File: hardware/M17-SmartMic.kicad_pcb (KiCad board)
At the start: 4 copper layers, 100 x 80 mm, 193 parts, among them IC301 LM4991xx, J301 CAT_TX, J302 CAT_TX, J401 Radio, J402 USB_C, J403 Radio_Opt, J404 Kenwood-3.5, J405 Kenwood-2.5, J406 OLED, J407 KH-RJ45-58-8P8C, J408 STLink, J409 UART, J410 Speaker, J411 +12V, Q201 MMBT3904, Q202 IRLML2244, Q301 IRLML2060, Q302 BSS138, Q303 BSS138, SW201 Button Power, SW202 Reset, SW203 Button Enter, SW204 Button Left, SW205 Button Up, SW206 Button Down, SW207 Button Escape, SW208 Button Right, U201 STM32F405RGTx, U202 TPS7A2033, U203 TP6841S6, U301 MCP6002, U302 MAX9814, U401 USBLC6-2, U501 MCP4551-103, U502 MCP455x, U503 MCP6002, U504 MCP6002, Y201 8 MHz

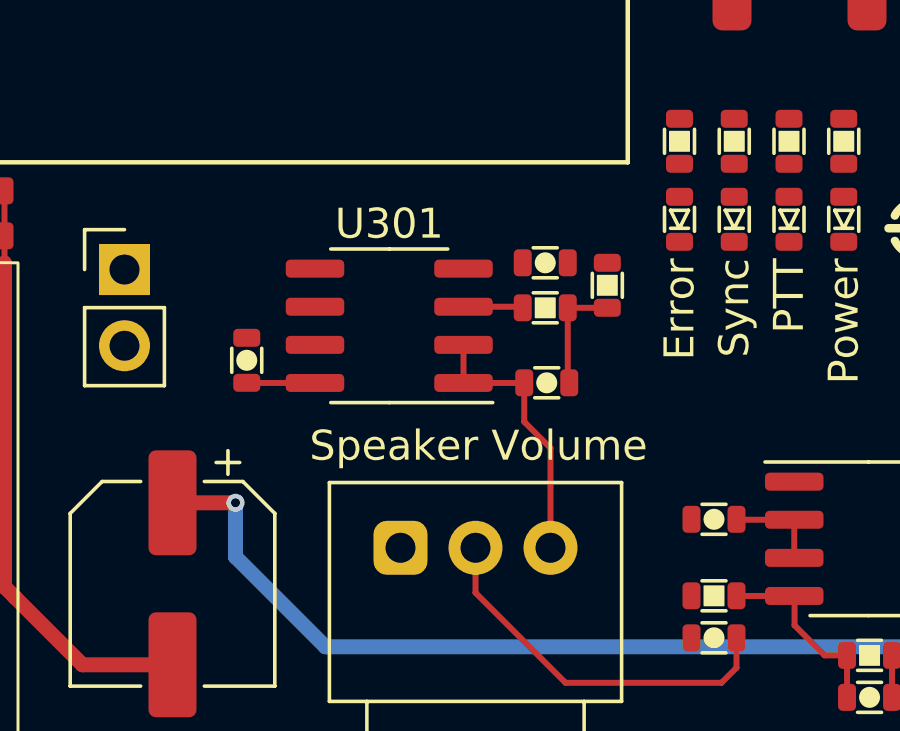
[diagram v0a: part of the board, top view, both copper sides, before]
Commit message: Updated audio output stage
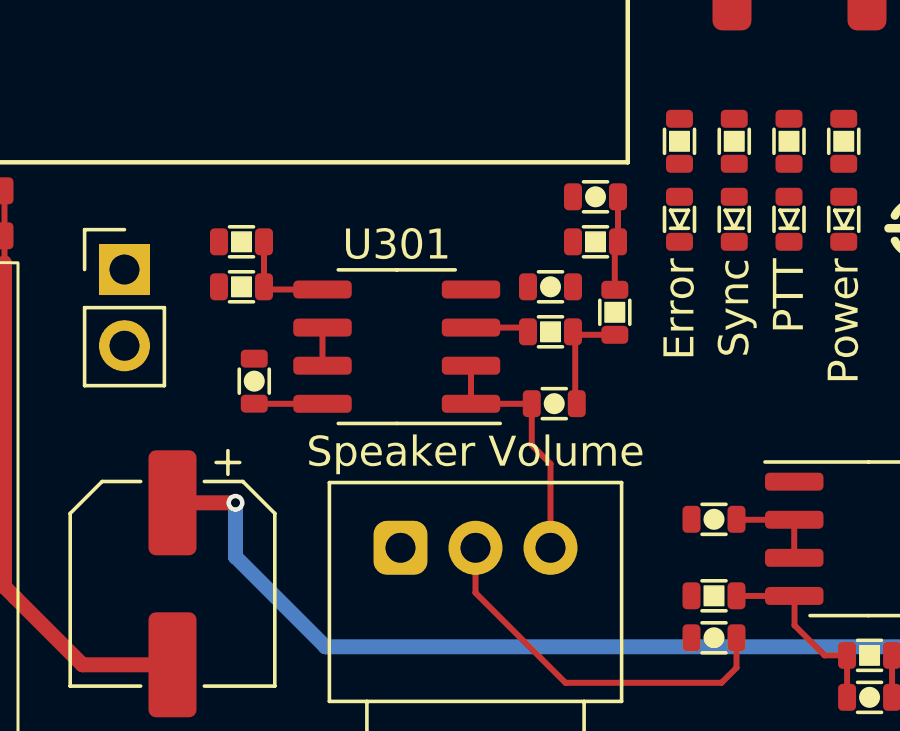
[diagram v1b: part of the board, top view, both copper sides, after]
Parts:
- added C315: 4u7, pkl_dipol:C_0603, F.Cu at (136.5, 120.8)
- added R316: 9k1, pkl_dipol:R_0603, F.Cu at (136.5, 122.3)
- added R317: 10k, pkl_dipol:R_0603, F.Cu at (124.7, 122.3)
- added R318: 10k, pkl_dipol:R_0603, F.Cu at (124.7, 123.8)
- C303: value 4.7n -> 220n
- C304: value 10n -> 1u5
- R303: value 7.5k -> 130k
- R304: value 4.7k -> 36k
- R307: value 1k8 -> 3k3
- moved R303 0.93 mm to (137.1, 124.7)
- moved C303 0.82 mm to (135.0, 123.8)
- moved R304 0.82 mm to (135.0, 125.3)
- moved U301 0.74 mm to (129.9, 125.8)
- moved C302 0.74 mm to (125.1, 126.9)
- moved C304 0.74 mm to (135.1, 127.7)
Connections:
- R303 pad 1: AUDIO_SPK -> Net-(C315-Pad1)
- U301 pad 5: unconnected-(U301B-+-Pad5) -> Net-(U301B-+)
- U301 pad 6: unconnected-(U301B---Pad6) -> Net-(U301B--)
- U301 pad 7: unconnected-(U301-Pad7) -> Net-(U301B--)
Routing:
- net Net-(U301B-+): track 0.00 -> 3.49 mm
- net Net-(C315-Pad1): track 0.00 -> 3.14 mm
- net Net-(U301B--): track 0.00 -> 1.27 mm
- net Net-(U301A--): track 9.16 -> 8.36 mm

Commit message: PCB Layout
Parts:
- added C226: 100n, pkl_dipol:C_0603, F.Cu at (75.0, 102.1)
- added C227: 10n, pkl_dipol:C_0603, F.Cu at (75.0, 103.5)
- added FB204: FB0805, pkl_dipol:L_0805, F.Cu at (68.8, 102.9)
- added FB401: FB0805, pkl_dipol:L_0805, F.Cu at (111.9, 75.3)
- added JP201: Jumper_2_Bridged, Connector_PinHeader_2.54mm:PinHeader_1x02_P2.54mm_Vertical, F.Cu at (101.9, 84.4)
- added L202: 5u, pkl_dipol:L_0805, F.Cu at (205.8, 63.9)
- J302: value CAT_TX -> CAT_RX
- moved TP303 143.0 mm to (37.4, 107.2)
- moved TP304 142.8 mm to (28.0, 102.8)
- moved TP501 134.3 mm to (33.1, 104.5)
- moved TP502 128.5 mm to (29.9, 106.0)
- moved R202 120.0 mm to (207.0, 87.0)
- moved C223 80.3 mm to (210.0, 63.7)
- moved TP301 67.2 mm to (122.8, 149.6)
- moved FB201 62.4 mm to (124.7, 75.6), turned to 0 degrees
- moved TP302 40.1 mm to (123.0, 153.4)
- moved J410 28.0 mm to (92.8, 125.2), turned to 90 degrees
- moved C301 27.6 mm to (81.0, 97.0)
- moved Q301 27.6 mm to (78.4, 97.0)
- moved R301 27.6 mm to (83.1, 96.2)
- moved R302 27.6 mm to (83.1, 97.8)
- moved TP504 22.0 mm to (35.2, 97.3)
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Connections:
- C213 pad 1: VDD -> /MCU & Power/VDD_MCU
- C214 pad 1: VDD -> /MCU & Power/VDD_MCU
- C216 pad 1: VDD -> /MCU & Power/VDD_MCU
- C217 pad 1: VDD -> /MCU & Power/VDD_MCU
- C219 pad 1: VDD -> /MCU & Power/VDD_MCU
- C221 pad 1: VDD -> /MCU & Power/VDD_MCU
- C222 pad 1: VDD -> /MCU & Power/VDD_MCU
- C223 pad 1: VAA -> Net-(JP201-A)
- D203 pad 1: +5V -> Net-(D203-K)
- D401 pad 1: +5V -> Net-(D401-K)
- FB201 pad 1: +12V -> Net-(Q202-S)
- FB201 pad 2: Net-(Q202-D) -> VIN
- Q202 pad 2: VIN -> Net-(Q202-S)
- Q202 pad 3: Net-(Q202-D) -> +12V
- R205 pad 1: VIN -> Net-(Q202-S)
- SW201 pad 1: VIN -> Net-(Q202-S)
- U201 pad 1: VBAT -> unconnected-(U201-VBAT-Pad1)
- U201 pad 19: VDD -> /MCU & Power/VDD_MCU
- U201 pad 32: VDD -> /MCU & Power/VDD_MCU
- U201 pad 48: VDD -> /MCU & Power/VDD_MCU
- U201 pad 64: VDD -> /MCU & Power/VDD_MCU
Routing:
- net BTN_DOWN: track 0.00 -> 94.9 mm, vias 0 -> 2
- net BTN_LEFT: track 0.00 -> 91.2 mm, vias 0 -> 2
- net BTN_RIGHT: track 0.00 -> 87.8 mm, vias 0 -> 2
- net ~{BOOT0}: track 0.00 -> 83.3 mm, vias 0 -> 2
- net BTN_UP: track 0.00 -> 76.9 mm, vias 0 -> 2
- net BTN_ENT: track 0.00 -> 72.0 mm, vias 0 -> 2
- net SPK_MUTE: track 0.00 -> 70.6 mm, vias 0 -> 2
- net ~{PTT_IN}: track 2.90 -> 69.0 mm, vias 0 -> 3
- net AUDIO_SPK: track 0.00 -> 64.9 mm, vias 0 -> 2
- net LED-ERROR: track 0.00 -> 63.0 mm, vias 0 -> 2
- net VDD: track 3.87 -> 65.8 mm
- net LED-SYNC: track 0.00 -> 60.9 mm, vias 0 -> 2
- net LED-PTT: track 0.00 -> 58.8 mm, vias 0 -> 2
- net USB_DN: track 0.00 -> 57.5 mm
- net USB_DP: track 0.00 -> 56.8 mm
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- added copper zone on F.Cu, net GND

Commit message: PCB Layout [WIP]
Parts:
- moved C223 137.9 mm to (75.7, 94.8), turned to 180 degrees
- moved R201 137.6 mm to (78.9, 82.2), turned to 0 degrees
- moved C211 135.3 mm to (80.3, 94.5), turned to -90 degrees
- moved C209 134.8 mm to (79.7, 91.7), turned to 90 degrees
- moved L202 133.3 mm to (75.7, 92.7), turned to 180 degrees
- moved C206 129.3 mm to (83.4, 94.7), turned to 180 degrees
- moved R204 127.9 mm to (82.1, 83.5), turned to 90 degrees
- moved U202 127.8 mm to (83.6, 91.8), turned to 180 degrees
- moved R202 127.8 mm to (79.4, 80.1), turned to -90 degrees
- moved D202 127.0 mm to (82.3, 80.3), turned to 0 degrees
- moved Q201 126.9 mm to (82.8, 86.7), turned to -90 degrees
- moved R203 125.1 mm to (83.5, 83.5), turned to -90 degrees
- moved C208 122.4 mm to (86.4, 92.0), turned to 90 degrees
- moved R206 121.8 mm to (85.4, 86.9), turned to -90 degrees
- moved R205 119.8 mm to (86.2, 84.7), turned to 180 degrees
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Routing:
- net BASEBAND_RX: track 0.00 -> 105.8 mm, vias 0 -> 2
- net I2C_SDA: track 0.00 -> 93.4 mm, vias 0 -> 3
- net I2C_SCL: track 0.00 -> 93.1 mm, vias 0 -> 3
- net BASEBAND_TX: track 0.00 -> 92.4 mm, vias 0 -> 2
- net Net-(Q202-S): track 7.96 -> 64.3 mm, vias 0 -> 4
- net RADIO_PTT: track 0.00 -> 48.0 mm, vias 0 -> 1
- net SWDIO: track 0.00 -> 36.9 mm, vias 0 -> 2
- net SWCLK: track 0.00 -> 31.6 mm, vias 0 -> 2
- net USART1_RX: track 0.00 -> 30.9 mm, vias 0 -> 1
- net USART1_TX: track 0.00 -> 28.6 mm, vias 0 -> 1
- net /Baseband/BB_RX_W: track 0.00 -> 19.3 mm
- net /Baseband/BB_RX_A: track 0.00 -> 19.2 mm
- net Net-(C508-Pad1): track 0.00 -> 17.2 mm, vias 0 -> 2
- net /Baseband/BB_TX_W: track 0.00 -> 17.1 mm
- net +5V: track 23.0 -> 10.3 mm
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- removed copper zone on F.Cu, net VIN

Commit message: PCB Layout [WIP]
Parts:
- moved TP502 70.5 mm to (100.3, 109.5)
- moved TP501 70.0 mm to (102.9, 109.7)
- moved TP503 70.0 mm to (103.2, 73.7)
- moved TP504 65.2 mm to (96.2, 74.3)
- moved TP303 63.8 mm to (96.8, 130.5)
- moved TP302 51.2 mm to (75.2, 134.8)
- moved TP304 43.0 mm to (68.2, 117.8)
- moved C510 42.0 mm to (137.9, 77.0)
- moved TP301 27.6 mm to (140.7, 128.7)
- moved C224 24.2 mm to (102.0, 81.0), turned to -90 degrees
- moved C512 24.0 mm to (137.8, 70.2), turned to -90 degrees
- moved FB203 23.3 mm to (99.7, 80.5)
- moved C225 22.7 mm to (103.5, 81.0), turned to -90 degrees
- moved R506 20.8 mm to (146.4, 67.0), turned to -90 degrees
- moved C507 15.9 mm to (146.4, 70.8), turned to -90 degrees
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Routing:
- net Net-(R201-Pad1): track 7.96 -> 122.1 mm, vias 0 -> 2
- net RADIO_TX: track 6.10 -> 76.6 mm, vias 0 -> 2
- net CAT_RXin: track 17.9 -> 67.7 mm, vias 0 -> 1
- net CAT_TXout: track 6.77 -> 55.8 mm, vias 0 -> 1
- net Net-(Q202-S): track 64.3 -> 111.0 mm, vias 4 -> 6
- net Net-(C510-Pad2): track 0.00 -> 42.3 mm, vias 0 -> 2
- net GPIO_POWER: track 1.97 -> 38.5 mm, vias 0 -> 2
- net NRST: track 46.9 -> 79.2 mm, vias 2 -> 0
- net RADIO_RX: track 9.41 -> 34.2 mm
- net Net-(C505-Pad1): track 1.40 -> 17.5 mm, vias 0 -> 2
- net RADIO_PTT: track 48.0 -> 32.9 mm, vias 1 -> 0
- net SPEAKER: track 54.3 -> 41.7 mm
- net I2C_SDA: track 93.4 -> 103.9 mm
- net I2C_SCL: track 93.1 -> 103.2 mm
- net /Baseband/BB_RX_W: track 19.3 -> 28.9 mm
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
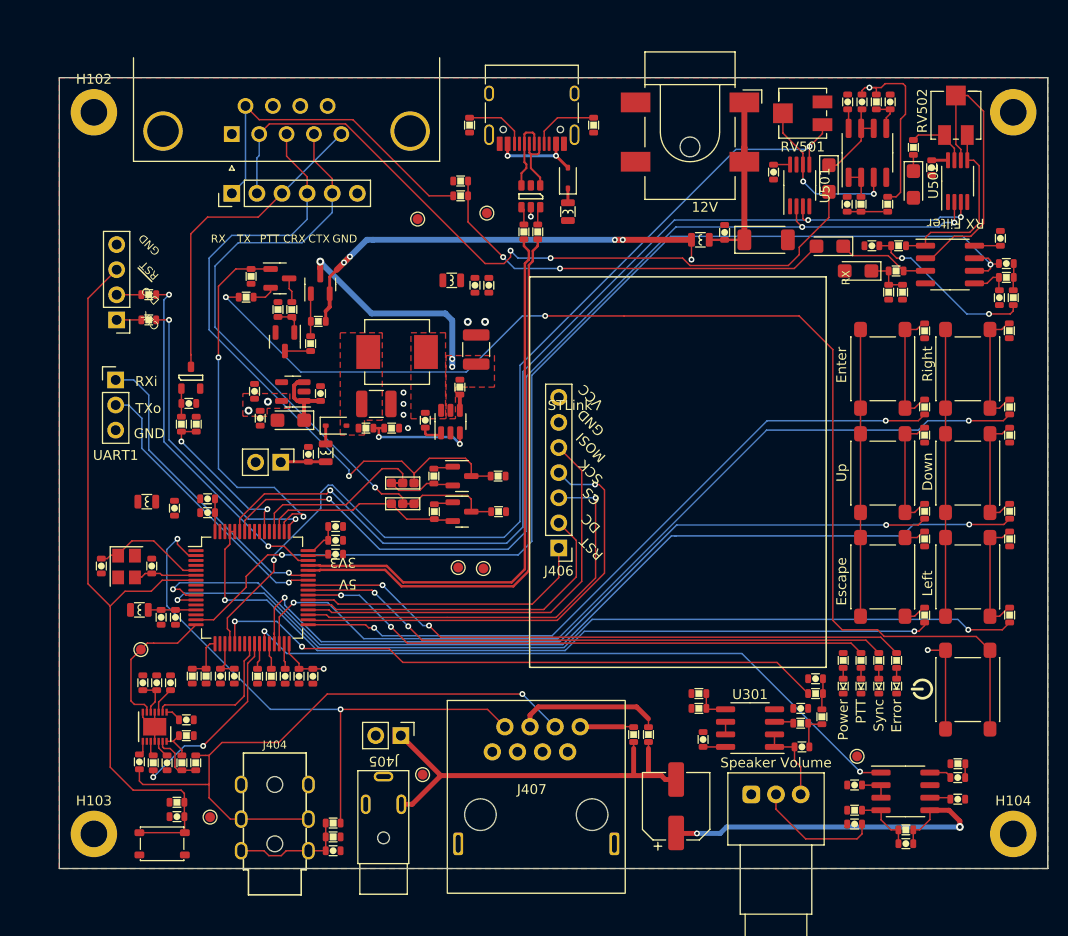
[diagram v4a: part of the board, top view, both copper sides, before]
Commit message: PCB Layout [WIP] + HMI connector
Added ZIF connector for HMI, updated reset button reference, added backup power connector for RTC + general layout progress
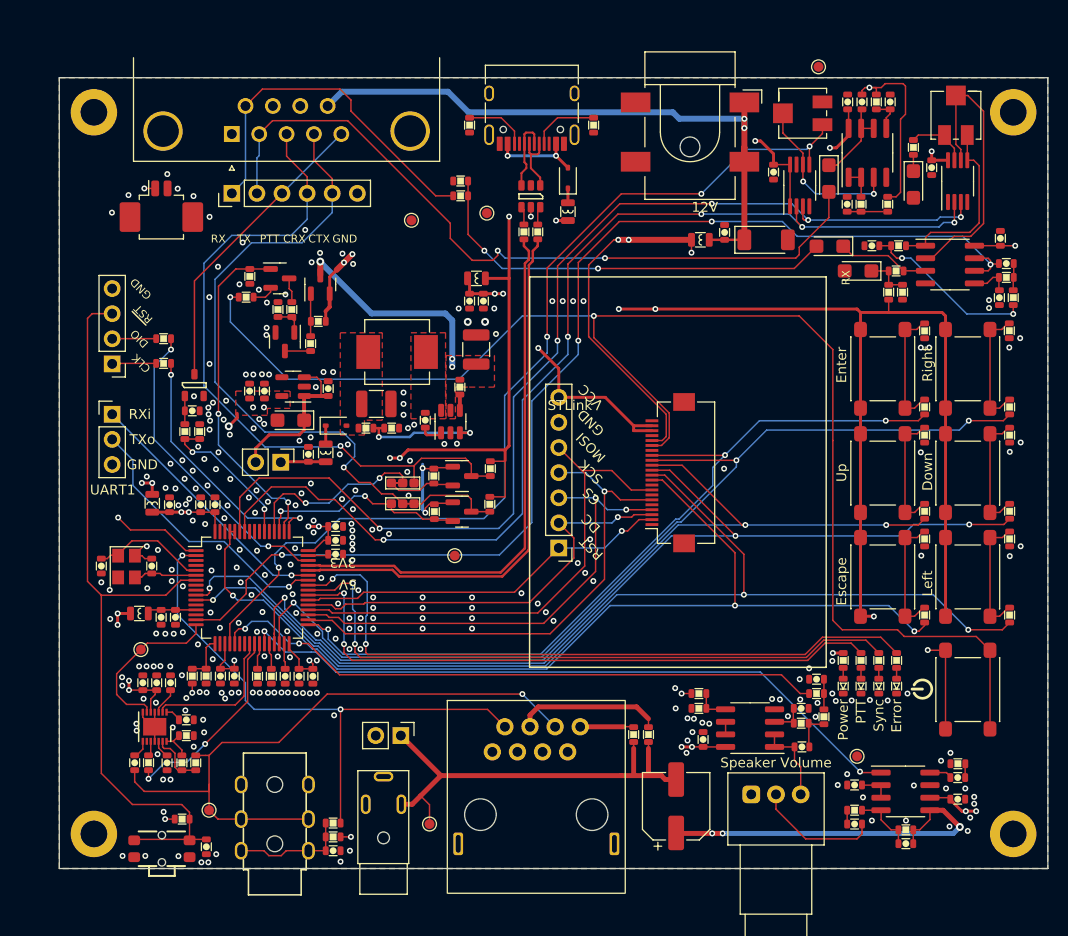
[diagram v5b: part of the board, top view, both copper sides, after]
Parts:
- added J412: Hirose FH12-22S-0.5SH(55), Connector_FFC-FPC:Hirose_FH12-22S-0.5SH_1x22-1MP_P0.50mm_Horizontal, F.Cu at (121.8, 100.0)
- added J413: Molex 532610271, Connector_Molex:Molex_PicoBlade_53261-0271_1x02-1MP_P1.25mm_Horizontal, F.Cu at (70.3, 73.6)
- SW202: footprint pkl_buttons_switches:SW_SPST_3x4x2.5 -> M17_misc_passive:SW_SPST_436351045816
- moved TP502 62.4 mm to (136.8, 58.9)
- moved TP303 5.05 mm to (97.5, 135.5)
- moved R408 4.70 mm to (70.5, 86.4)
- moved R407 4.65 mm to (70.5, 88.9)
- moved J408 4.47 mm to (65.3, 89.0)
- moved C215 4.26 mm to (74.9, 137.8), turned to 90 degrees
- moved J409 3.49 mm to (65.3, 94.0)
- moved TP501 3.18 mm to (100.0, 108.3)
- moved C211 2.95 mm to (79.2, 91.7), turned to 90 degrees
- moved FB203 2.51 mm to (102.2, 80.3), turned to 0 degrees
- moved R214 1.78 mm to (72.4, 135.0)
- moved C224 1.69 mm to (101.5, 82.6)
- moved C225 1.69 mm to (102.9, 82.6)
- moved R306 1.16 mm to (103.5, 103.2), turned to -90 degrees
- moved C227 1.10 mm to (75.8, 103.2), turned to 90 degrees
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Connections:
- net Net-(Q202-S) renamed HMI_VIN
- net Net-(R201-Pad1) renamed HMI_PWR_ON
- FB401 pad 1: Net-(D401-K) -> +5V
- FB401 pad 2: +5V -> Net-(D401-K)
- SW202 pad 1: GND -> NRST
- SW202 pad 2: NRST -> GND
- U201 pad 1: unconnected-(U201-VBAT-Pad1) -> +BATT
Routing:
- net VDD: track 69.2 -> 325.8 mm, vias 2 -> 21
- net +5V: track 10.3 -> 228.0 mm, vias 1 -> 7
- net VAA: track 6.68 -> 139.0 mm, vias 0 -> 7
- net +BATT: track 0.00 -> 47.6 mm, vias 0 -> 2
- net /MCU & Power/VDD_MCU: track 16.7 -> 64.3 mm, vias 1 -> 6
- net VIN: track 18.9 -> 63.7 mm, vias 0 -> 2
- net HMI_VIN: track 111.0 -> 137.5 mm
- net ~{BOOT0}: track 82.7 -> 102.4 mm, vias 2 -> 3
- net HMI_PWR_ON: track 122.1 -> 140.8 mm
- net BTN_LEFT: track 90.5 -> 107.6 mm, vias 2 -> 3
- net BTN_UP: track 77.4 -> 91.1 mm, vias 2 -> 3
- net BTN_RIGHT: track 88.1 -> 99.0 mm, vias 2 -> 3
- net BTN_ENT: track 72.1 -> 82.7 mm, vias 2 -> 3
- net BTN_DOWN: track 95.5 -> 104.8 mm, vias 2 -> 3
- net OLED_RST: track 29.6 -> 38.1 mm, vias 0 -> 1
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- added copper zone on B.Cu, net GND
- added copper zone on In2.Cu, net GND
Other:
- board text removed: "RX Filter"

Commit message: Replaced pkl symbols with kicad library symbols
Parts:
- U401: value USBLC6-2 -> USBLC6-2SC6
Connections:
- net VIN renamed LINE
- D204 pad A: Net-(D204-PadA) -> (no net)
- D204 pad C: GND -> (no net)
- D205 pad A: Net-(D205-PadA) -> (no net)
- D205 pad C: GND -> (no net)
- D206 pad A: Net-(D206-PadA) -> (no net)
- D206 pad C: GND -> (no net)
- D207 pad A: Net-(D207-PadA) -> (no net)
- D207 pad C: GND -> (no net)
- R225 pad 1: Net-(D204-PadA) -> Net-(D204-A)
- R226 pad 1: Net-(D205-PadA) -> Net-(D205-A)
- R227 pad 1: Net-(D206-PadA) -> Net-(D206-A)
- R228 pad 1: Net-(D207-PadA) -> Net-(D207-A)
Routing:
- net Net-(D207-PadA): track 1.10 -> 0.00 mm
- net Net-(D207-A): track 0.00 -> 1.10 mm
- net Net-(D206-PadA): track 1.10 -> 0.00 mm
- net Net-(D206-A): track 0.00 -> 1.10 mm
- net Net-(D205-PadA): track 1.10 -> 0.00 mm
- net Net-(D205-A): track 0.00 -> 1.10 mm
- net Net-(D204-PadA): track 1.10 -> 0.00 mm
- net Net-(D204-A): track 0.00 -> 1.10 mm
